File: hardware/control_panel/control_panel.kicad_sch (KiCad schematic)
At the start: 6 parts, among them SW1 RotaryEncoder_Switch_MP, SW2 SW_Push

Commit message: KiCad updates and EC11 to TWT
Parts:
- removed SW1: RotaryEncoder_Switch_MP, Rotary_Encoder:RotaryEncoder_Alps_EC11E-Switch_Vertical_H20mm, symbol Device:RotaryEncoder_Switch_MP
- added 5VGND1: Conn_01x02_Pin, Connector_JST:JST_XH_B2B-XH-A_1x02_P2.50mm_Vertical, symbol Connector:Conn_01x02_Pin
- added RELAY_2CH_1: Conn_01x04_Pin, Connector_PinHeader_2.54mm:PinHeader_1x04_P2.54mm_Vertical, symbol Connector:Conn_01x04_Pin
- added ST7789_Socket1: Conn_01x08_Socket, Connector_PinSocket_2.54mm:PinSocket_1x08_P2.54mm_Horizontal, symbol Connector:Conn_01x08_Socket
- added U1: ~, symbol TMB_Library:SW_ThumbWheelToggle
- renumbered SW2 to SW_Cancel_Reset1
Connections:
- net GND: now also ESPMC1.GND, 5VGND1.2 (Pin_2), RELAY_2CH_1.1 (Pin_1), ST7789_Socket1.2 (Pin_2), ST7789_Socket1.8 (Pin_8), U1.C (COM)
- net IN1_FAN: now reaches ESPMC1.1 (GP1)
- net IN1_FAN: now also RELAY_2CH_1.2 (Pin_2)
- net LCD_RST: now reaches ESPMC1.10 (GP10)
- net LCD_RST: now also ST7789_Socket1.4 (Pin_4)
- net LCD_SDA: now reaches ESPMC1.11 (GP11)
- net LCD_SDA: now also ST7789_Socket1.5 (Pin_5)
- net LCD_SCL: now reaches ESPMC1.12 (GP12)
- net LCD_SCL: now also ST7789_Socket1.6 (Pin_6)
- net IN2_LEDS: now reaches ESPMC1.2 (GP2)
- net IN2_LEDS: now also RELAY_2CH_1.3 (Pin_3)
- net 3V3+: now reaches ESPMC1.3V3 (3V3(OUT))
- net 3V3+: now also RELAY_2CH_1.4 (Pin_4), ST7789_Socket1.7 (Pin_7)
- net at ESPMC1.5 (GP5): now also U1.3 (WH_DIR2)
- net at ESPMC1.5V: now also 5VGND1.1 (Pin_1)
- net at ESPMC1.6 (GP6): now also U1.2 (SW)
- net at ESPMC1.7 (GP7): now also U1.1 (WH_DIR1)
- net LCD_BL: now reaches ESPMC1.8 (GP8)
- net LCD_BL: now also ST7789_Socket1.1 (Pin_1)
- net LCD_DC: now reaches ESPMC1.9 (GP9)
- net LCD_DC: now also ST7789_Socket1.3 (Pin_3)
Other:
- moved on the sheet: R1, R2, R3, SW_Cancel_Reset1

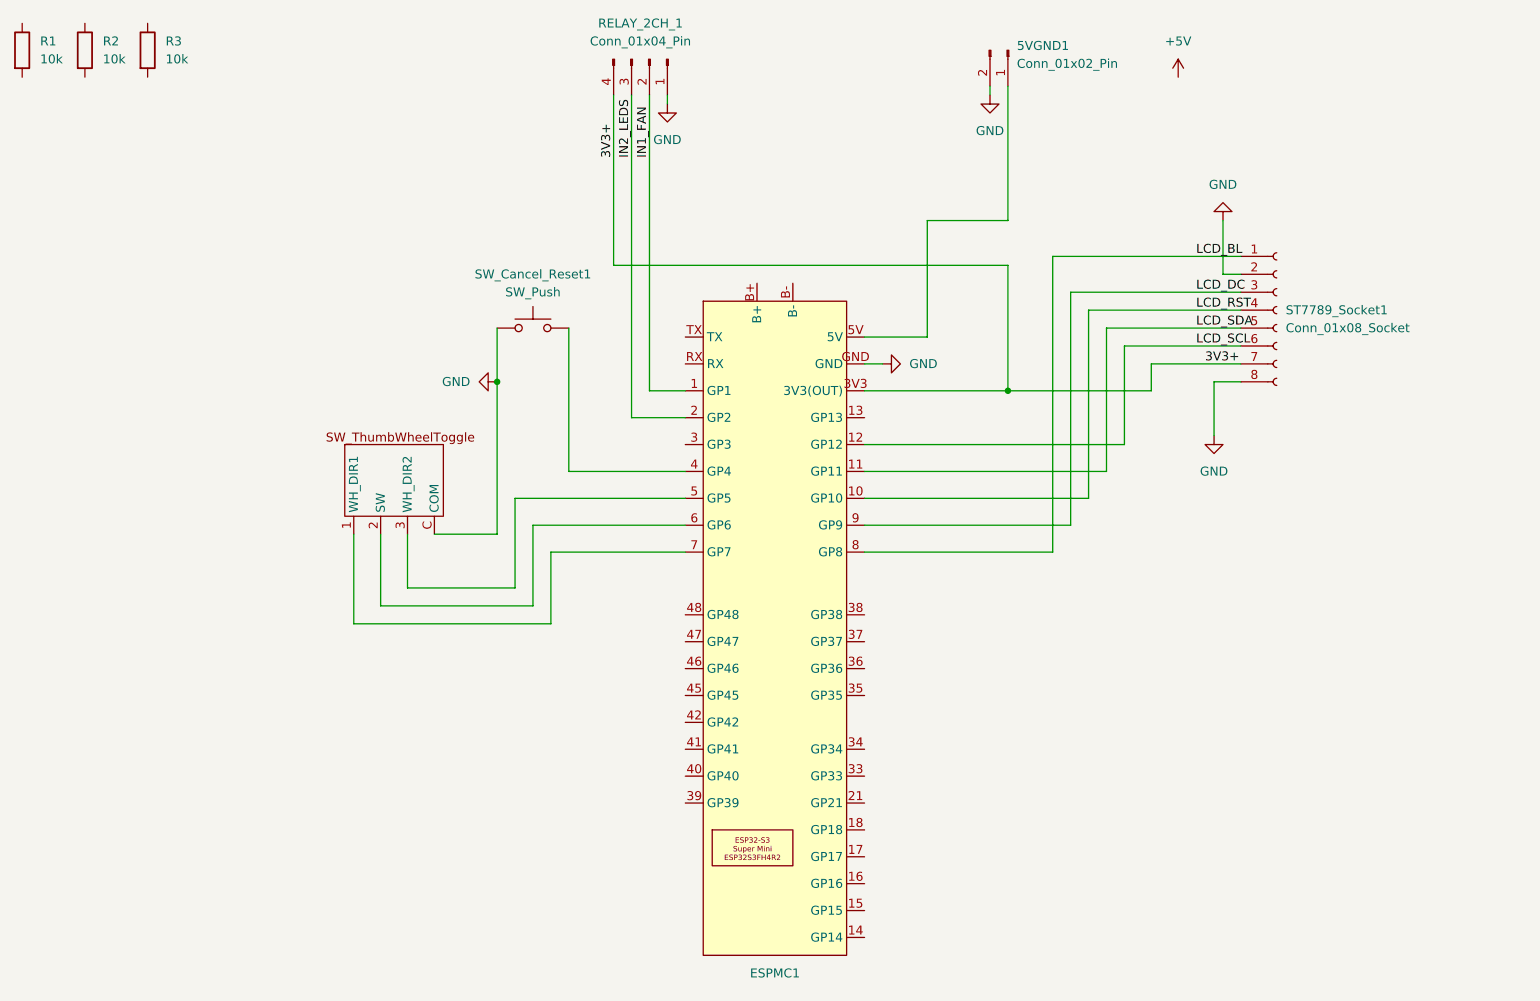
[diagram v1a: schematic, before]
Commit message: KiCad and python script for stitching PCB layers into one SVG for printing
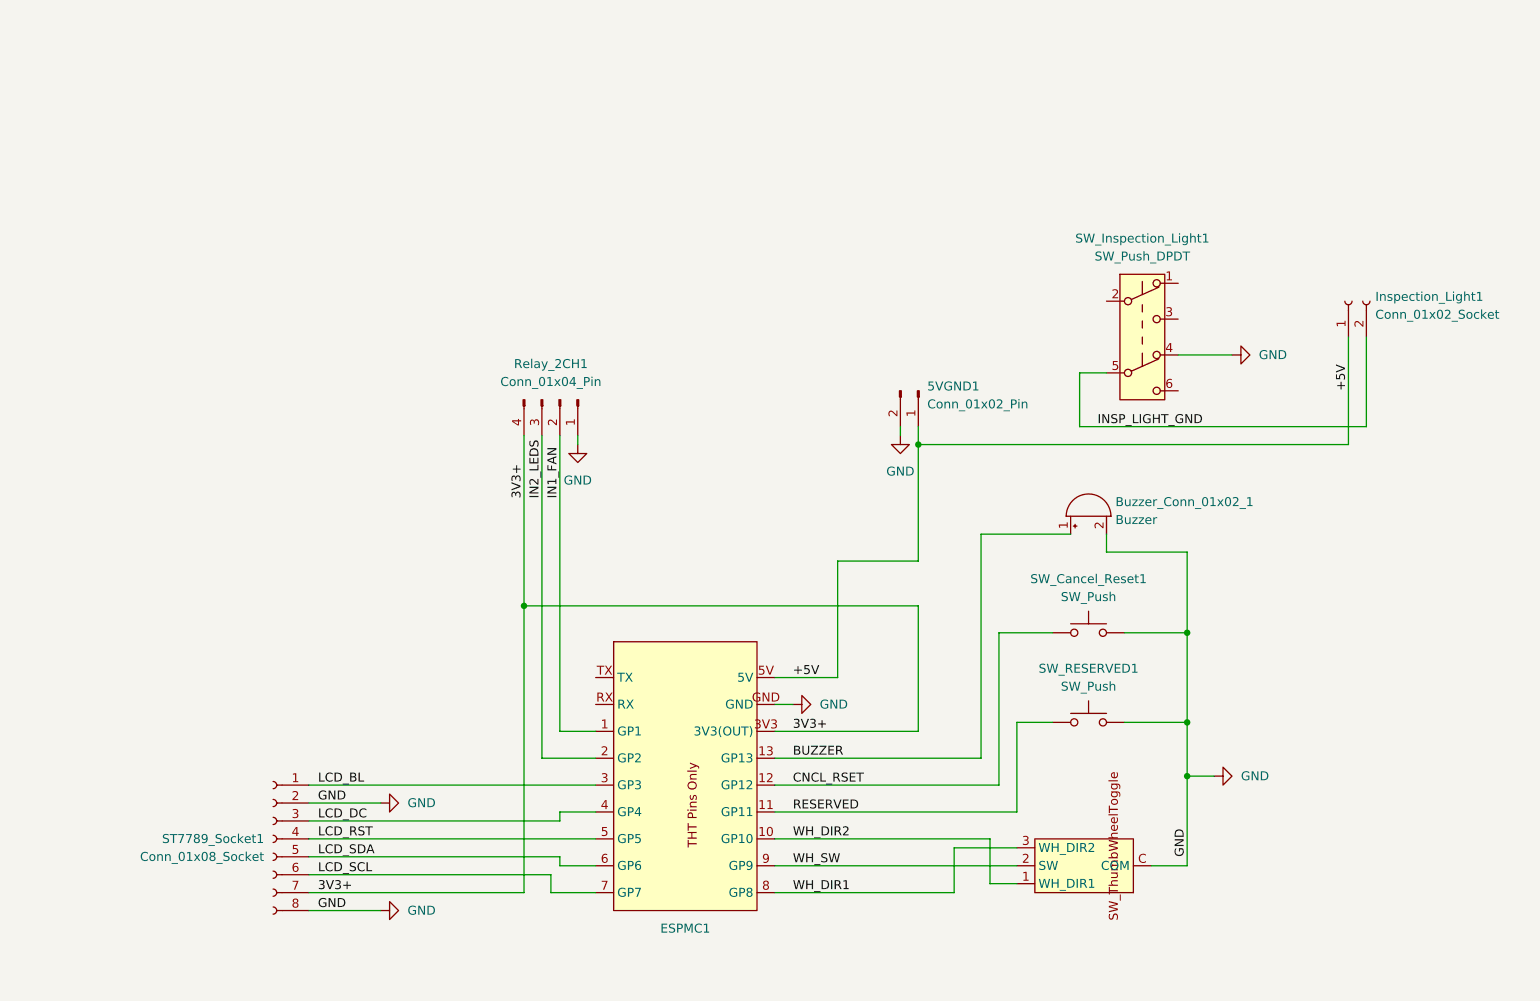
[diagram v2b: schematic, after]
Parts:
- removed R1, R2, R3: 10k, Resistor_THT:R_Axial_DIN0204_L3.6mm_D1.6mm_P5.08mm_Horizontal, symbol Device:R
- added Buzzer_Conn_01x02_1: Buzzer, Connector_PinHeader_2.54mm:PinHeader_1x02_P2.54mm_Vertical, symbol Device:Buzzer
- added Inspection_Light1: Conn_01x02_Socket, Connector_JST:JST_XH_B2B-XH-A_1x02_P2.50mm_Vertical, symbol Connector:Conn_01x02_Socket
- added SW_Cancel_Reset1: SW_Push, Button_Switch_THT:SW_PUSH_6mm_H8.5mm, symbol Switch:SW_Push
- added SW_Inspection_Light1: SW_Push_DPDT, TMB_Library:SW_Push_DPDT_8x8mm, symbol Switch:SW_Push_DPDT
- ESPMC1: footprint TMB_Library:ESP32-S3_Super_Mini -> TMB_Library:ESP32-S3_Super_Mini_THTONLY; symbol TMB_Library:ESP32-S3_Super_Mini -> TMB_Library:ESP32-S3_Super_Mini_THTONLY
- SW_TWT_Start_Pause_Adjust1: renamed from U1; footprint (none) -> TMB_Library:SW_ThumbWheelToggle
- renumbered RELAY_2CH_1 to Relay_2CH1, SW_Cancel_Reset1 to SW_RESERVED1
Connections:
- net +5V: now also 5VGND1.1 (Pin_1), ESPMC1.5V, Inspection_Light1.1 (Pin_1)
- net GND: now also SW_RESERVED1.2, Buzzer_Conn_01x02_1.2 (-), SW_Cancel_Reset1.2, SW_Inspection_Light1.4 (A); no longer SW_RESERVED1.1
- net LCD_BL: now also ESPMC1.3 (GP3); no longer ESPMC1.8 (GP8)
- net LCD_DC: now also ESPMC1.4 (GP4); no longer ESPMC1.9 (GP9)
- net LCD_RST: now also ESPMC1.5 (GP5); no longer ESPMC1.10 (GP10)
- net LCD_SCL: now also ESPMC1.7 (GP7); no longer ESPMC1.12 (GP12)
- net LCD_SDA: now also ESPMC1.6 (GP6); no longer ESPMC1.11 (GP11)
- net BUZZER: now reaches ESPMC1.13 (GP13)
- net BUZZER: now also Buzzer_Conn_01x02_1.1 (+)
- net WH_DIR1: now reaches SW_TWT_Start_Pause_Adjust1.3 (WH_DIR2)
- net WH_DIR1: now also ESPMC1.8 (GP8); no longer ESPMC1.5 (GP5)
- net WH_SW: now reaches SW_TWT_Start_Pause_Adjust1.2 (SW)
- net WH_SW: now also ESPMC1.9 (GP9); no longer ESPMC1.6 (GP6)
- net WH_DIR2: now reaches SW_TWT_Start_Pause_Adjust1.1 (WH_DIR1)
- net WH_DIR2: now also ESPMC1.10 (GP10); no longer ESPMC1.7 (GP7)
- new net CNCL_RSET: ESPMC1.12 (GP12), SW_Cancel_Reset1.1
- new net INSP_LIGHT_GND: Inspection_Light1.2 (Pin_2), SW_Inspection_Light1.5 (B)
- new net RESERVED: ESPMC1.11 (GP11), SW_RESERVED1.1
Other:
- moved on the sheet: 5VGND1, Relay_2CH1, ST7789_Socket1, SW_RESERVED1

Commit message: KiCad design fixes and Kicad pcb export fixes
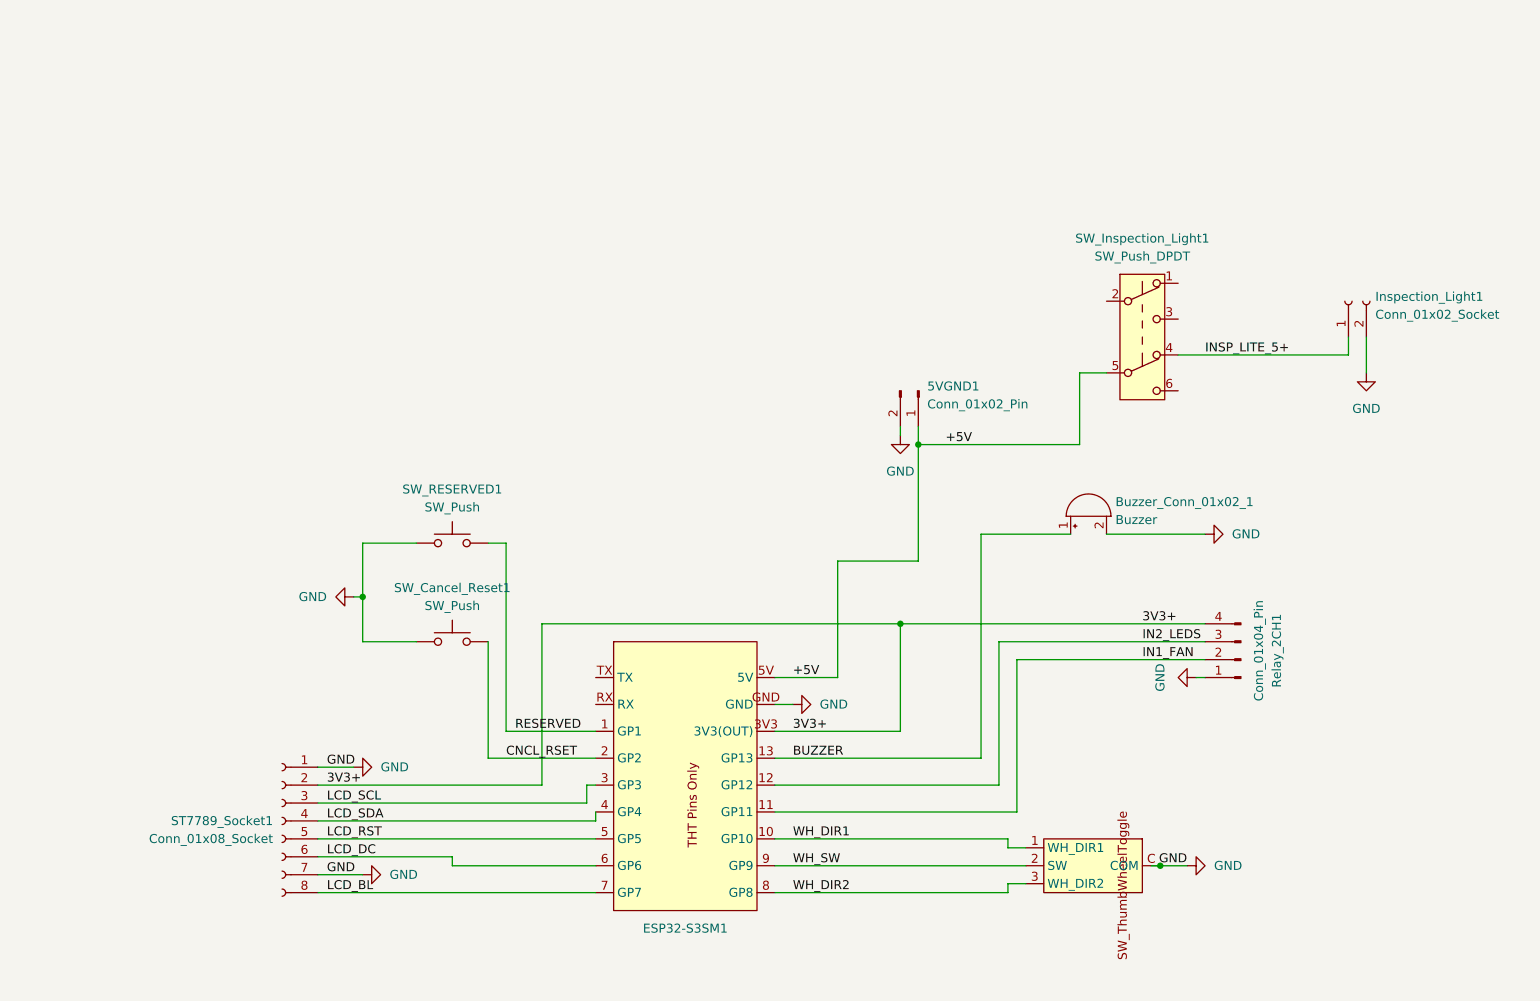
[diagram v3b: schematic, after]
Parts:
- Inspection_Light1: footprint Connector_JST:JST_XH_B2B-XH-A_1x02_P2.50mm_Vertical -> Connector_PinHeader_2.54mm:PinHeader_1x02_P2.54mm_Vertical
- renumbered ESPMC1 to ESP32-S3SM1
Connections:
- net +5V: now also SW_Inspection_Light1.5 (B); no longer Inspection_Light1.1 (Pin_1)
- net 3V3+: now also ST7789_Socket1.2 (Pin_2); no longer ST7789_Socket1.7 (Pin_7)
- net CNCL_RSET: now also ESP32-S3SM1.2 (GP2), SW_Cancel_Reset1.2; no longer ESP32-S3SM1.12 (GP12), SW_Cancel_Reset1.1
- net GND: now also Inspection_Light1.2 (Pin_2), ST7789_Socket1.1 (Pin_1), ST7789_Socket1.7 (Pin_7), SW_Cancel_Reset1.1, SW_RESERVED1.1; no longer ST7789_Socket1.2 (Pin_2), ST7789_Socket1.8 (Pin_8), SW_Cancel_Reset1.2, SW_Inspection_Light1.4 (A), SW_RESERVED1.2
- net IN1_FAN: now also ESP32-S3SM1.11 (GP11); no longer ESP32-S3SM1.1 (GP1)
- net IN2_LEDS: now also ESP32-S3SM1.12 (GP12); no longer ESP32-S3SM1.2 (GP2)
- net LCD_BL: now also ESP32-S3SM1.7 (GP7), ST7789_Socket1.8 (Pin_8); no longer ESP32-S3SM1.3 (GP3), ST7789_Socket1.1 (Pin_1)
- net LCD_DC: now also ESP32-S3SM1.6 (GP6), ST7789_Socket1.6 (Pin_6); no longer ESP32-S3SM1.4 (GP4), ST7789_Socket1.3 (Pin_3)
- net LCD_RST: now also ST7789_Socket1.5 (Pin_5); no longer ST7789_Socket1.4 (Pin_4)
- net LCD_SCL: now also ESP32-S3SM1.3 (GP3), ST7789_Socket1.3 (Pin_3); no longer ESP32-S3SM1.7 (GP7), ST7789_Socket1.6 (Pin_6)
- net LCD_SDA: now also ESP32-S3SM1.4 (GP4), ST7789_Socket1.4 (Pin_4); no longer ESP32-S3SM1.6 (GP6), ST7789_Socket1.5 (Pin_5)
- net RESERVED: now also ESP32-S3SM1.1 (GP1), SW_RESERVED1.2; no longer ESP32-S3SM1.11 (GP11), SW_RESERVED1.1
- net WH_DIR1: now also ESP32-S3SM1.10 (GP10), SW_TWT_Start_Pause_Adjust1.1 (WH_DIR1); no longer ESP32-S3SM1.8 (GP8), SW_TWT_Start_Pause_Adjust1.3 (WH_DIR2)
- net WH_DIR2: now also ESP32-S3SM1.8 (GP8), SW_TWT_Start_Pause_Adjust1.3 (WH_DIR2); no longer ESP32-S3SM1.10 (GP10), SW_TWT_Start_Pause_Adjust1.1 (WH_DIR1)
- removed net INSP_LIGHT_GND: Inspection_Light1.2 (Pin_2), SW_Inspection_Light1.5 (B)
- new net INSP_LITE_5+: Inspection_Light1.1 (Pin_1), SW_Inspection_Light1.4 (A)
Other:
- moved on the sheet: Relay_2CH1, ST7789_Socket1, SW_Cancel_Reset1, SW_RESERVED1

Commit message: Kicad - Mimimum Vias + 0.5mm min track width + script changes
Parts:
- removed SW_RESERVED1: SW_Push, Button_Switch_THT:SW_PUSH_6mm_H8.5mm, symbol Switch:SW_Push
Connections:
- net RESERVED: no longer names the net of ESP32-S3SM1.1 (GP1)
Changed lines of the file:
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@@
-	)
-	(junction
-		(at 69.85 101.6)
-		(diameter 0)
-		(color 0 0 0 0)
 	)
 	(junction
@@
 	(wire
 		(pts
-			(xy 69.85 93.98) (xy 77.47 93.98)
-		)
-		(stroke
-			(width 0)
-			(type default)
-		)
-	)
-	(wire
-		(pts
 			(xy 148.59 80.01) (xy 171.45 80.01)
 		)
@@
 	(wire
 		(pts
-			(xy 90.17 93.98) (xy 90.17 120.65)
-		)
-		(stroke
-			(width 0)
-			(type default)
-		)
-	)
-	(wire
-		(pts
 			(xy 128.27 132.08) (xy 162.56 132.08)
 		)
@@
 	(wire
 		(pts
-			(xy 69.85 93.98) (xy 69.85 101.6)
-		)
-		(stroke
-			(width 0)
-			(type default)
-		)
-	)
-	(wire
-		(pts
 			(xy 95.25 128.27) (xy 95.25 105.41)
 		)
@@
 	(wire
 		(pts
-			(xy 87.63 93.98) (xy 90.17 93.98)
-		)
-		(stroke
-			(width 0)
-			(type default)
-		)
-	)
-	(wire
-		(pts
 			(xy 148.59 96.52) (xy 137.16 96.52)
 		)
@@
 		(pts
 			(xy 146.05 77.47) (xy 146.05 78.74)
-		)
-		(stroke
-			(width 0)
-			(type default)
-		)
-	)
-	(wire
-		(pts
-			(xy 90.17 120.65) (xy 102.87 120.65)
 		)
 		(stroke
@@
 		)
 	)
-	(label "RESERVED"
-		(at 91.44 120.65 0)
-		(effects
-			(font
-				(size 1.27 1.27)
-			)
-			(justify left bottom)
-		)
-	)
 	(label "BUZZER"
 		(at 130.81 124.46 0)
@@
 		)
 	)
-	(symbol
-		(lib_id "Switch:SW_Push")
-		(at 82.55 93.98 0)
-		(unit 1)
-		(exclude_from_sim no)
-		(in_bom yes)
-		(on_board yes)
-		(dnp no)
-		(fields_autoplaced yes)
-		(property "Reference" "SW_RESERVED1"
-			(at 82.55 86.36 0)
-			(effects
-				(font
-					(size 1.27 1.27)
-				)
-			)
-		)
-		(property "Value" "SW_Push"
-			(at 82.55 88.9 0)
-			(effects
-				(font
-					(size 1.27 1.27)
-				)
-			)
-		)
-		(property "Footprint" "Button_Switch_THT:SW_PUSH_6mm_H8.5mm"
-			(at 82.55 88.9 0)
-			(effects
-				(font
-					(size 1.27 1.27)
-				)
-				(hide yes)
-			)
-		)
-		(property "Datasheet" "~"
-			(at 82.55 88.9 0)
-			(effects
-				(font
-					(size 1.27 1.27)
-				)
-				(hide yes)
-			)
-		)
-		(property "Description" "Push button switch, generic, two pins"
-			(at 82.55 93.98 0)
-			(effects
-				(font
-					(size 1.27 1.27)
-				)
-				(hide yes)
-			)
-		)
-		(pin "1"
-		)
-		(pin "2"
-		)
-		(instances
-			(project ""
-				(path "/59452313-4d2e-433c-bd3a-a836d98d9b68"
-					(reference "SW_RESERVED1")
-					(unit 1)
-				)
-			)
-		)
-	)
